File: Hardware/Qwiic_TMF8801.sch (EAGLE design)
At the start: 18 parts, among them J1 QWIIC_RIGHT_ANGLE, J2 QWIIC_RIGHT_ANGLE, U1 TMF8801

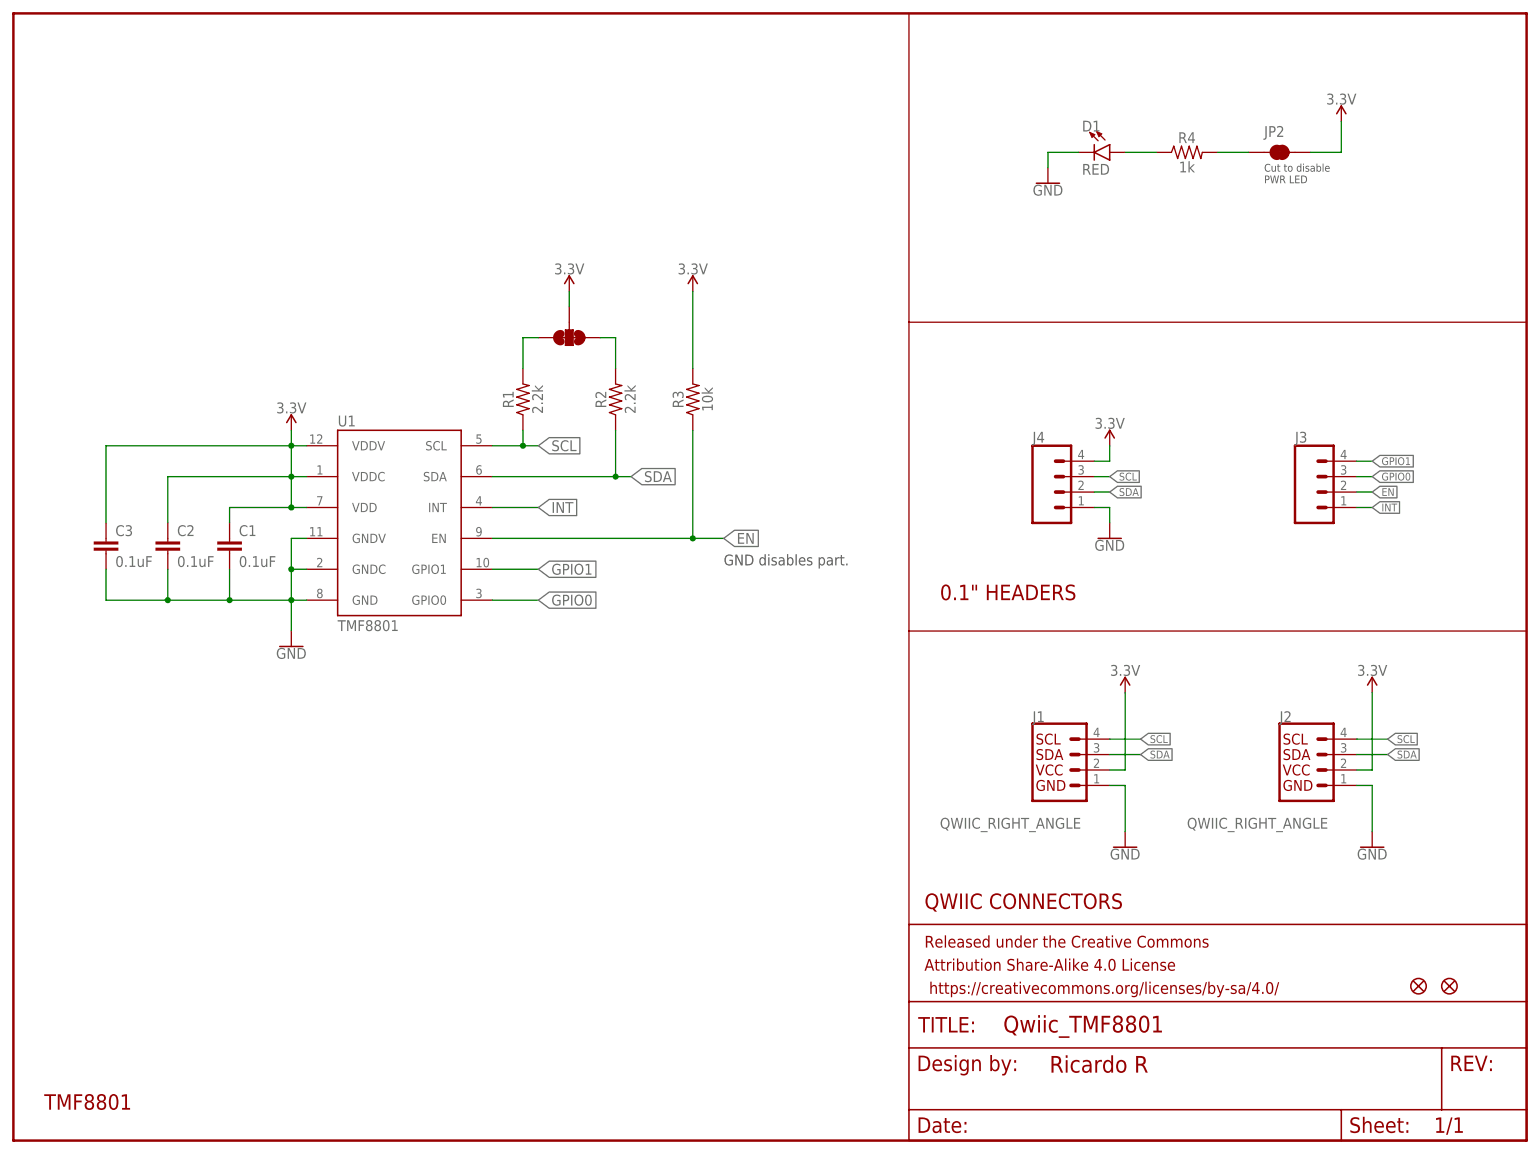
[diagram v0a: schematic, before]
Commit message: Add files via upload
Updated SCH file per Nathan's feedback
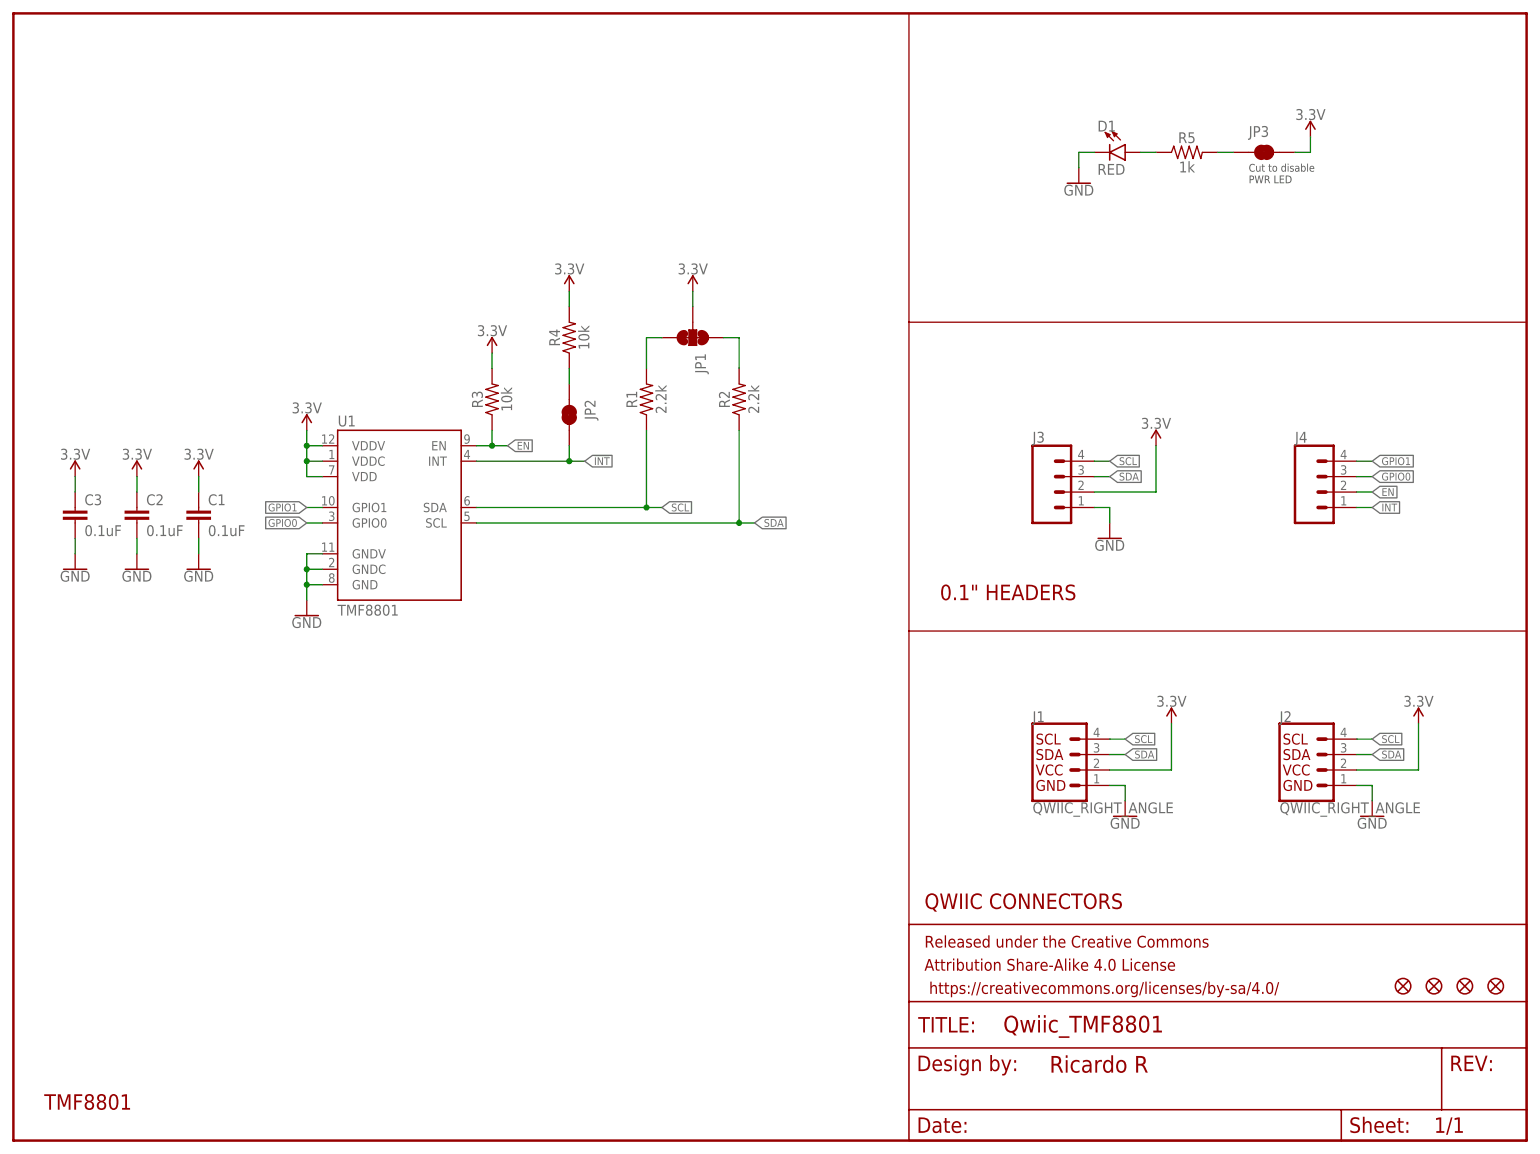
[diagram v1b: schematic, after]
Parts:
- added FD3, FD4: FIDUCIAL1X2, SparkFun-Aesthetics:FIDUCIAL1X2
- added JP3: JUMPER-SMT_2_NC_TRACE_SILK, SparkFun-Jumpers:JUMPER-SMT_2_NC_TRACE_SILK
- added R5: 1k, SparkFun-Resistors:1KOHM-0603-1/10W-1%
- C1, C2, C3: device SparkFun-Capacitors:0.1UF-0603-25V-5% -> SparkFun-Capacitors:0.1UF-0603-25V-(+80/-20%)
- J3, J4: device SparkFun-Connectors:CONN_04 -> SparkFun-Connectors:CONN_041X04_NO_SILK
- R4: value 1k -> 10k; device SparkFun-Resistors:1KOHM-0603-1/10W-1% -> SparkFun-Resistors:10KOHM-0603-1/10W-1%
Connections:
- new net !INT: JP2.2, U1.INT
- new net N$5: JP2.1, R4.1
- net 3.3V: now also J1.2, J2.2, J3.2, JP3.2, R4.2; no longer J1.VCC, J2.VCC, J4.4, JP2.2
- net EN: now also J4.2; no longer J3.2
- net GND: now also J1.1, J2.1, J3.1; no longer J1.GND, J2.GND, J4.1
- net GPIO0: now also J4.3; no longer J3.3
- net GPIO1: now also J4.4; no longer J3.4
- net INT: now also J4.1; no longer J3.1, U1.INT
- net N$1: now also R5.1; no longer R4.1
- net N$4: now also JP3.1, R5.2; no longer JP2.1, R4.2
- net SCL: now also J1.4, J2.4, J3.4, U1.SDA; no longer J1.SCL, J2.SCL, J4.3, U1.SCL
- net SDA: now also J1.3, J2.3, J3.3, U1.SCL; no longer J1.SDA, J2.SDA, J4.2, U1.SDA
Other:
- note removed: "GND disables part."
- moved on the sheet: C1, C2, C3, D1, JP2, R1, R2, R3, R4, U1

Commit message: Add files via upload
Added missing libraries and labels; changed design per Nathan's feedback and SparfFun design guidelines
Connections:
- removed net INT: J4.1
- net !INT: now also J4.4
- net EN: now also J4.1; no longer J4.2
- net GPIO1: now also J4.2; no longer J4.4
